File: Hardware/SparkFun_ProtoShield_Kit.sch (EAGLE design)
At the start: 27 parts

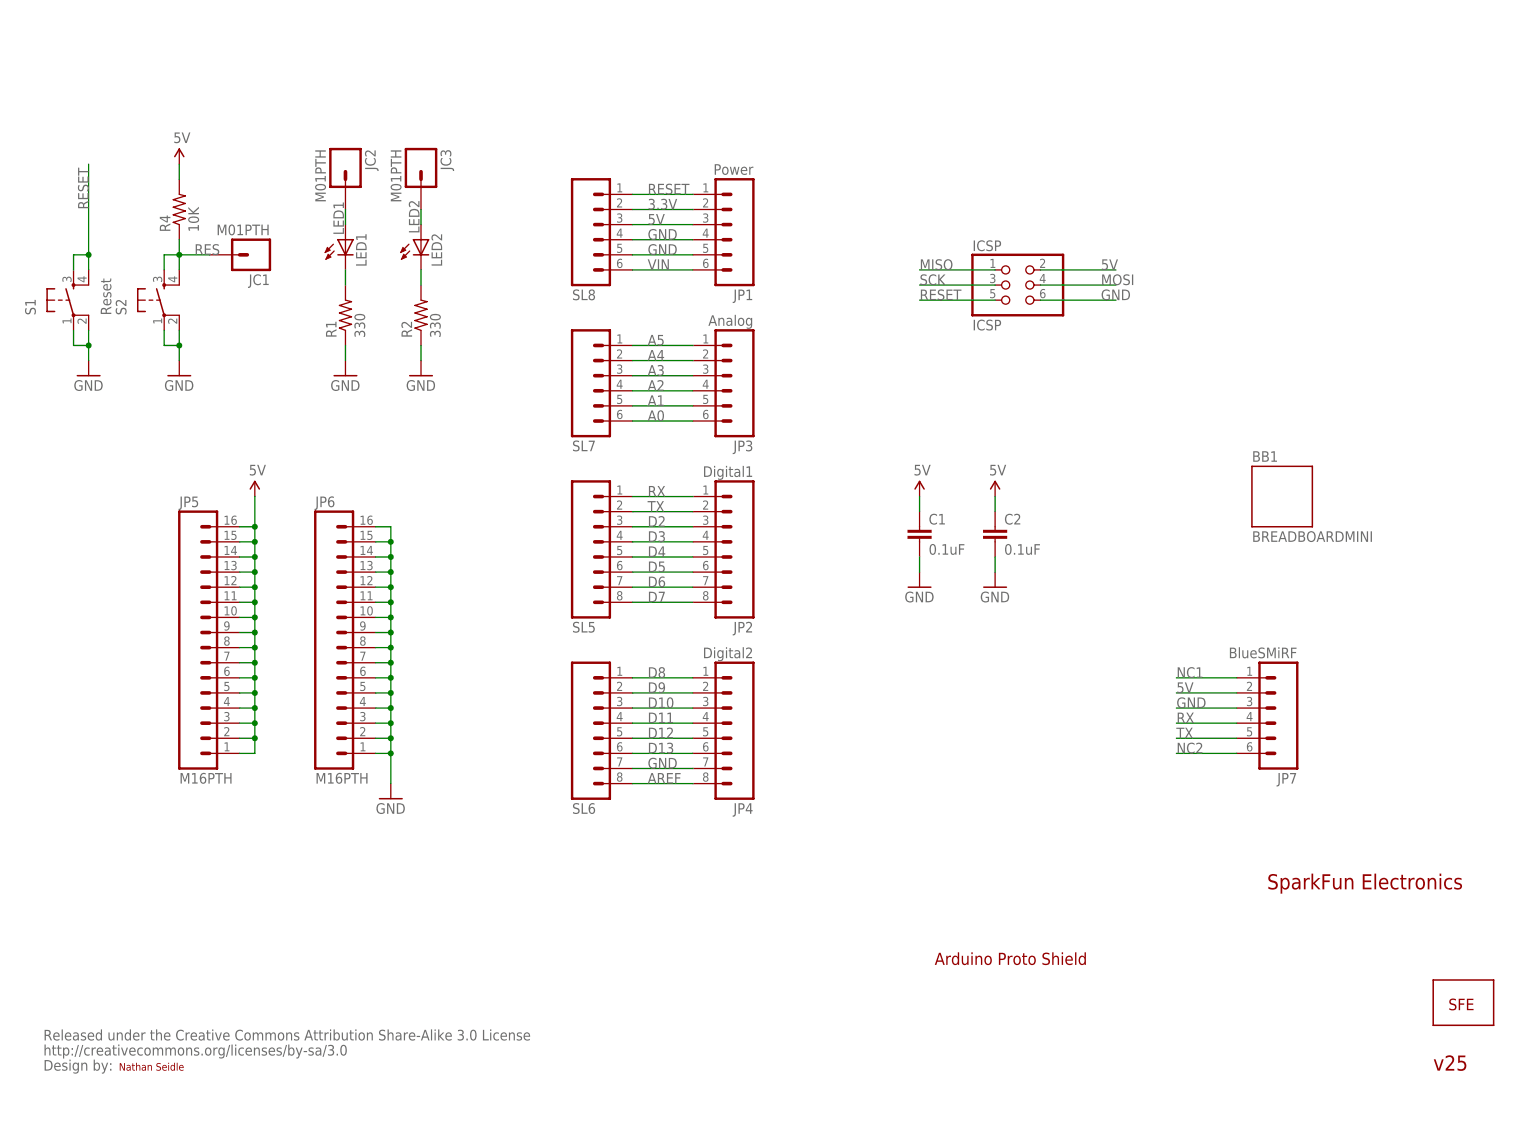
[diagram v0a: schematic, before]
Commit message: WIP - basic hardware layout changes
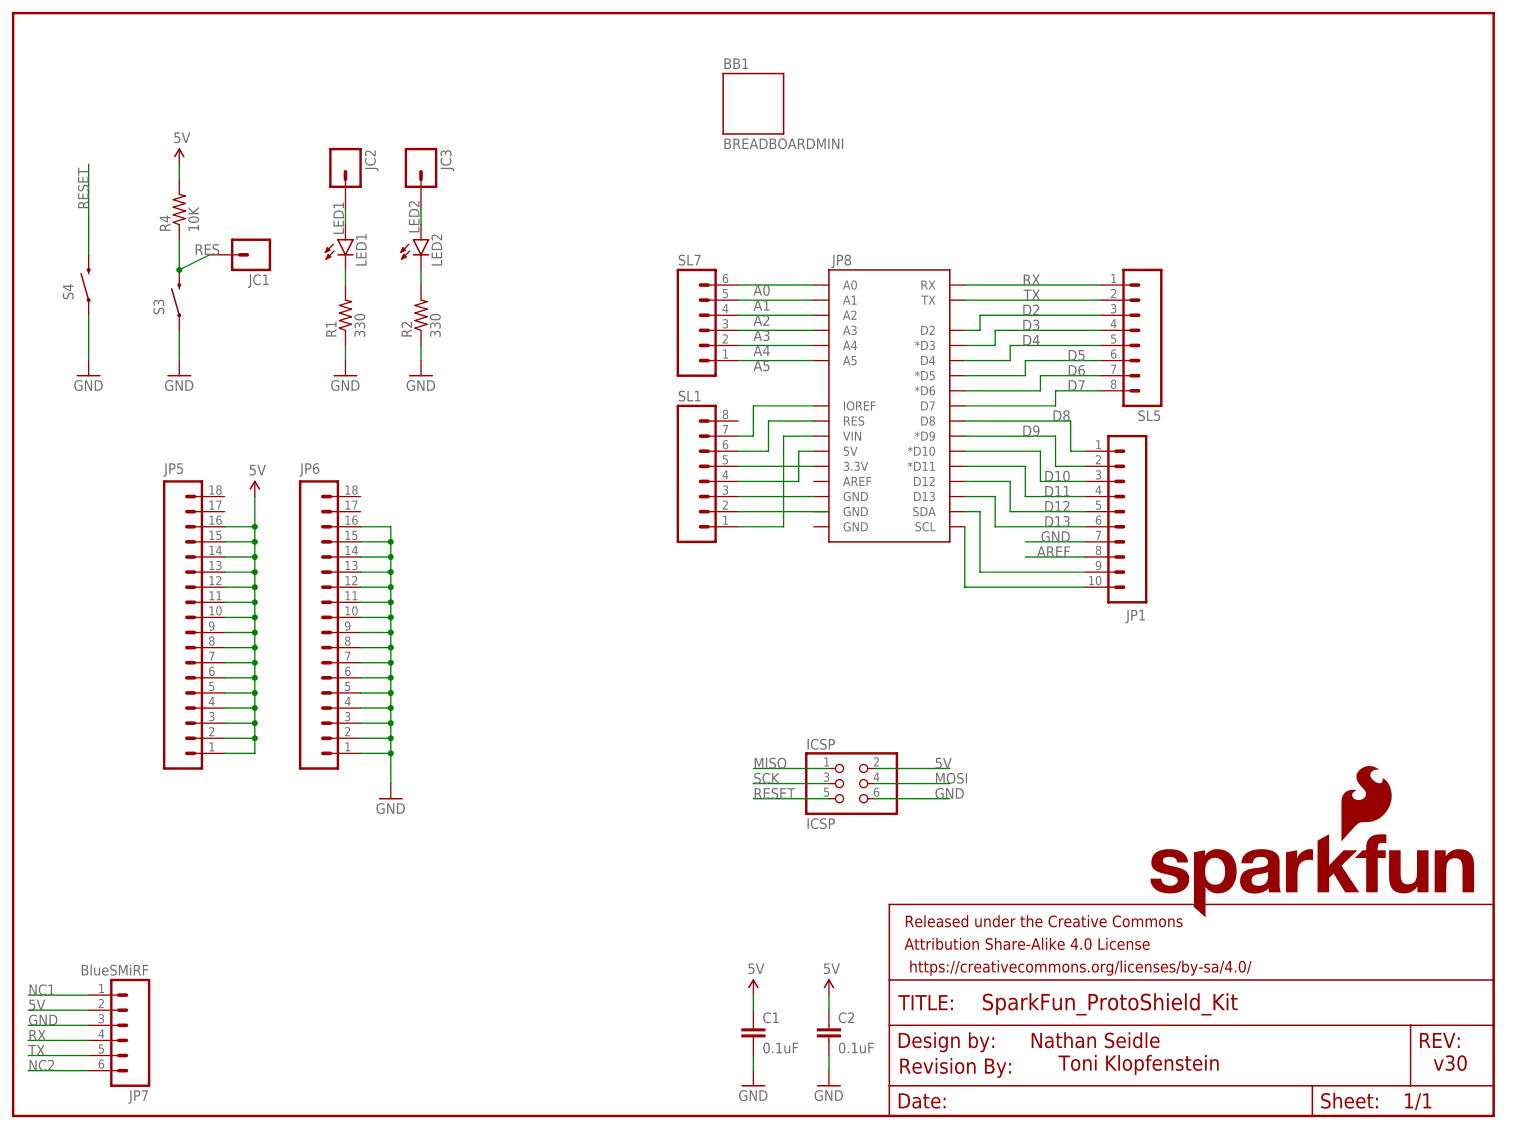
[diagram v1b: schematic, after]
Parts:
- removed JP2: Digital1, SparkFun:M08
- removed JP3: Analog, SparkFun:M06SIP
- removed JP4: Digital2, SparkFun:M08
- removed S1: Reset, SparkFun:TAC_SWITCHPTH
- removed S2: (no value), SparkFun:TAC_SWITCHPTH
- removed SL6: (no value), SparkFun:M08
- removed SL8: (no value), SparkFun:M06SIP
- added FRAME1: FRAME-LETTER, SparkFun-Aesthetics:FRAME-LETTER
- added JP8: ARDUINO_R3_SHIELDR3_PROTO_SHIELD, TempLibrary:ARDUINO_R3_SHIELDR3_PROTO_SHIELD
- added S3, S4: SWITCH-MOMENTARY-2PTH, SparkFun-Electromechanical:SWITCH-MOMENTARY-2PTH
- added SL1: (no value), SparkFun:M08
- JC1, JC2, JC3: value M01PTH -> (none); device SparkFun:M01PTH -> SparkFun-Connectors:M01PTH
- JP1: value Power -> (none); device SparkFun:M06SIP -> SparkFun-Connectors:M10SILK_FEMALE_PTH
- JP5, JP6: value M16PTH -> (none); device SparkFun:M16PTH -> TempLibrary:M18"
- LED1, LED2: device SparkFun:LED5MM -> SparkFun-LED:LED3MM
- U$1: value LOGO-SFENEW -> SFE_LOGO_NAME_FLAME.1_INCH; device SparkFun:LOGO-SFENEW -> SparkFun-Aesthetics:SFE_LOGO_NAME_FLAME.1_INCH
- U$2: value CREATIVE_COMMONS -> REVISION; device SparkFun:CREATIVE_COMMONS -> SparkFun-Aesthetics:REVISION
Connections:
- removed net 3.3V: JP1.2, SL8.2
- removed net VIN: JP1.6, SL8.6
- new net N$1: JP8.IOREF, SL1.7
- new net N$183: JP8.GND@2, SL1.3
- new net N$184: SL1.2
- new net N$185: JP8.VIN, SL1.1
- new net N$186: JP1.9, JP8.SDA
- new net N$187: JP1.10, JP8.SCL
- new net N$2: JP8.RES, SL1.6
- new net N$8: JP8.3.3V, SL1.5
- new net N$9: JP8.5V, SL1.4
- net 5V: no longer JP1.3, SL8.3
- net A0: now also JP8.A0; no longer JP3.6
- net A1: now also JP8.A1; no longer JP3.5
- net A2: now also JP8.A2; no longer JP3.4
- net A3: now also JP8.A3; no longer JP3.3
- net A4: now also JP8.A4; no longer JP3.2
- net A5: now also JP8.A5; no longer JP3.1
- net AREF: now also JP1.8; no longer JP4.8, SL6.8
- net D10: now also JP1.3, JP8.*D10; no longer JP4.3, SL6.3
- net D11: now also JP1.4, JP8.*D11; no longer JP4.4, SL6.4
- net D12: now also JP1.5, JP8.D12; no longer JP4.5, SL6.5
- net D13: now also JP1.6, JP8.D13; no longer JP4.6, SL6.6
- net D2: now also JP8.D2; no longer JP2.3
- net D3: now also JP8.*D3; no longer JP2.4
- net D4: now also JP8.D4; no longer JP2.5
- net D5: now also JP8.*D5; no longer JP2.6
- net D6: now also JP8.*D6; no longer JP2.7
- net D7: now also JP8.D7; no longer JP2.8
- net D8: now also JP1.1, JP8.D8; no longer JP4.1, SL6.1
- net D9: now also JP1.2, JP8.*D9; no longer JP4.2, SL6.2
- net GND: now also JP1.7, S3.1, S4.1; no longer JP1.4, JP1.5, JP4.7, S1.1, S1.2, S2.1, S2.2, SL6.7, SL8.4, SL8.5
- net RES: now also S3.2; no longer S2.3, S2.4
- net RESET: now also S4.2; no longer JP1.1, S1.3, S1.4, SL8.1
- net RX: now also JP8.RX; no longer JP2.1
- net TX: now also JP8.TX; no longer JP2.2
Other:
- note added: "Toni Klopfenstein"
- note added: "v30"
- note removed: "Arduino Proto Shield"
- note removed: "SparkFun Electronics"
- note removed: "v25"
- moved on the sheet: BB1, C1, C2, ICSP, JP7, SL5, SL7

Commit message: Ready for engineering review
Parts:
- added LOGO1: OSHW-LOGOS, SparkFun-Aesthetics:OSHW-LOGOS
- added SJ1, SJ2, SJ3, SJ4: JUMPER-PAD-2-NC_BY_TRACE, SparkFun-Passives:JUMPER-PAD-2-NC_BY_TRACE
- JP5, JP6: device TempLibrary:M18" -> SparkFun-Connectors:M191X19
- U$1: value SFE_LOGO_NAME_FLAME.1_INCH -> SFE_LOGO_NAME.1_INCH; device SparkFun-Aesthetics:SFE_LOGO_NAME_FLAME.1_INCH -> SparkFun-Aesthetics:SFE_LOGO_NAME.1_INCH
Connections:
- net N$186 renamed SDA
- net N$187 renamed SCL
- removed net N$183: JP8.GND@2, SL1.3
- removed net N$184: SL1.2
- new net N$219: JP7.3, SJ3.1
- new net N$220: JP7.2, SJ4.1
- new net NC3: SL1.8
- net 5V: now also JP5.17, JP5.18, JP5.19, JP8.5V, SJ4.2, SL1.4; no longer JP7.2
- net AREF: now also JP8.AREF
- net GND: now also JP6.17, JP6.18, JP6.19, JP8.GND@0, JP8.GND@1, JP8.GND@2, SJ3.2, SL1.2, SL1.3; no longer JP7.3
- net N$2: now also JP7.5, SJ1.1; no longer JP8.RES, SL1.6
- net N$9: now also JP7.4, SJ2.1; no longer JP8.5V, SL1.4
- net RESET: now also JP8.RES, SL1.6
- net RX: now also SJ2.2; no longer JP7.4
- net TX: now also SJ1.2; no longer JP7.5
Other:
- note added: "Arduino Connections"
- note added: "Arduino Headers Connections"
- note added: "BlueSMiRF Footprint"
- note added: "Breadboard Footprint"
- note added: "Disable jumpers 1-4 to create customizable 6-pin header for prototyping."
- note added: "Prototyping Hardware"
- moved on the sheet: BB1, C1, C2, ICSP, JC1, JC2, JC3, JP1, JP7, JP8, LED1, LED2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

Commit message: Fixing part names, adding additional connector from engineering review
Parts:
- removed C1, C2: 0.1uF, SparkFun:CAPPTH2
- removed SL1, SL5: (no value), SparkFun:M08
- removed SL7: (no value), SparkFun:M06SIP
- added JP10, JP2: (no value), SparkFun-Connectors:M06SILK_FEMALE_PTH
- added JP11, JP12: (no value), SparkFun-Connectors:M08
- JP7: device SparkFun:M06SIP -> SparkFun-Connectors:M06SILK_FEMALE_PTH
- renumbered JC1 to JP3, JC2 to JP4, JC3 to JP9
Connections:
- removed net N$2: JP7.5, SJ1.1
- removed net N$219: JP7.3, SJ3.1
- removed net N$220: JP7.2, SJ4.1
- removed net N$9: JP7.4, SJ2.1
- new net FTDI_5V: JP2.2, JP7.2, SJ4.1
- new net FTDI_GND: JP2.3, JP7.3, SJ3.1
- new net FTDI_RX: JP2.4, JP7.4, SJ2.1
- new net FTDI_TX: JP2.5, JP7.5, SJ1.1
- net 5V: now also JP11.4; no longer C1.1, C2.1, SL1.4
- net A0: now also JP10.6; no longer SL7.6
- net A1: now also JP10.5; no longer SL7.5
- net A2: now also JP10.4; no longer SL7.4
- net A3: now also JP10.3; no longer SL7.3
- net A4: now also JP10.2; no longer SL7.2
- net A5: now also JP10.1; no longer SL7.1
- net D2: now also JP12.3; no longer SL5.3
- net D3: now also JP12.4; no longer SL5.4
- net D4: now also JP12.5; no longer SL5.5
- net D5: now also JP12.6; no longer SL5.6
- net D6: now also JP12.7; no longer SL5.7
- net D7: now also JP12.8; no longer SL5.8
- net GND: now also JP11.2, JP11.3; no longer C1.2, C2.2, SL1.2, SL1.3
- net N$1: now also JP11.7; no longer SL1.7
- net N$185: now also JP11.1; no longer SL1.1
- net N$8: now also JP11.5; no longer SL1.5
- net NC1: now also JP2.1
- net NC2: now also JP2.6
- net NC3: now also JP11.8; no longer SL1.8
- net RESET: now also JP11.6; no longer SL1.6
- net RX: now also JP12.1; no longer SL5.1
- net TX: now also JP12.2; no longer SL5.2
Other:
- moved on the sheet: BB1, JP7, SJ1, SJ2, SJ3, SJ4

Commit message: Updates from engineering review
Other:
- moved on the sheet: JP2, JP7, SJ1, SJ2, SJ3, SJ4

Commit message: Updates from checklist
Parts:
- BB1: device SparkFun:BREADBOARDMINI -> SparkFun-Boards:BREADBOARDMINI
- ICSP: device pinhead:PINHD-2X3 -> SparkFun-Connectors:AVR_SPI_PRG_6PTH
- R1, R2, R4: device SparkFun:RESISTORPTH1 -> SparkFun-Resistors:RESISTORAXIAL-0.3
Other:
- moved on the sheet: S3
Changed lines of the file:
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@@
 <?xml version="1.0" encoding="utf-8"?>
 <!DOCTYPE eagle SYSTEM "eagle.dtd">
-<eagle version="7.4.0">
+<eagle version="7.5.0">
 <drawing>
 <settings>
@@
 </classes>
 <parts>
-<part name="ICSP" library="pinhead" deviceset="PINHD-2X3" device="" value="ICSP"/>
-<part name="R1" library="SparkFun" deviceset="RESISTOR" device="PTH1" value="330"/>
-<part name="R2" library="SparkFun" deviceset="RESISTOR" device="PTH1" value="330"/>
+<part name="ICSP" library="SparkFun-Connectors" deviceset="AVR_SPI_PRG_6" device="PTH" value="ICSP"/>
+<part name="R1" library="SparkFun-Resistors" deviceset="RESISTOR" device="AXIAL-0.3" value="330"/>
+<part name="R2" library="SparkFun-Resistors" deviceset="RESISTOR" device="AXIAL-0.3" value="330"/>
 <part name="LED1" library="SparkFun-LED" deviceset="LED" device="3MM"/>
 <part name="LED2" library="SparkFun-LED" deviceset="LED" device="3MM"/>
@@
 <part name="P+2" library="SparkFun-Aesthetics" deviceset="5V" device="" value="5V"/>
 <part name="GND4" library="SparkFun-Aesthetics" deviceset="GND" device=""/>
-<part name="BB1" library="SparkFun" deviceset="BREADBOARD" device="MINI"/>
-<part name="R4" library="SparkFun" deviceset="RESISTOR" device="PTH1" value="10K"/>
+<part name="BB1" library="SparkFun-Boards" deviceset="BREADBOARD" device="MINI"/>
+<part name="R4" library="SparkFun-Resistors" deviceset="RESISTOR" device="AXIAL-0.3" value="10K"/>
 <part name="GND5" library="SparkFun-Aesthetics" deviceset="GND" device=""/>
 <part name="JP3" library="SparkFun-Connectors" deviceset="M01" device="PTH"/>
@@
 </plain>
 <instances>
-<instance part="ICSP" gate="A" x="33.02" y="60.96"/>
+<instance part="ICSP" gate="G$1" x="33.02" y="60.96"/>
 <instance part="R1" gate="G$1" x="226.06" y="109.22" smashed="yes" rot="R90">
 <attribute name="NAME" x="224.5614" y="105.41" size="1.778" layer="95" rot="R90"/>
@@
 <instance part="JP11" gate="G$1" x="12.7" y="124.46"/>
 <instance part="JP1" gate="G$1" x="101.6" y="111.76" rot="R180"/>
-<instance part="S3" gate="G$1" x="198.12" y="111.76" smashed="yes" rot="R90">
-<attribute name="NAME" x="195.58" y="109.22" size="1.778" layer="95" rot="R90"/>
+<instance part="S3" gate="G$1" x="198.12" y="109.22" smashed="yes" rot="R90">
+<attribute name="NAME" x="195.58" y="106.68" size="1.778" layer="95" rot="R90"/>
 </instance>
 <instance part="S4" gate="G$1" x="71.12" y="68.58" smashed="yes" rot="R90">
@@
 </segment>
 <segment>
-<wire x1="198.12" y1="106.68" x2="198.12" y2="101.6" width="0.1524" layer="91"/>
+<wire x1="198.12" y1="104.14" x2="198.12" y2="101.6" width="0.1524" layer="91"/>
 <pinref part="GND5" gate="1" pin="GND"/>
 <pinref part="S3" gate="G$1" pin="1"/>
 </segment>
 <segment>
-<wire x1="38.1" y1="58.42" x2="50.8" y2="58.42" width="0.1524" layer="91"/>
-<pinref part="ICSP" gate="A" pin="6"/>
+<wire x1="43.18" y1="58.42" x2="50.8" y2="58.42" width="0.1524" layer="91"/>
+<pinref part="ICSP" gate="G$1" pin="6"/>
 <pinref part="GND10" gate="1" pin="GND"/>
 <wire x1="50.8" y1="58.42" x2="50.8" y2="55.88" width="0.1524" layer="91"/>
@@
 <net name="RESET" class="0">
 <segment>
-<wire x1="30.48" y1="58.42" x2="17.78" y2="58.42" width="0.1524" layer="91"/>
-<pinref part="ICSP" gate="A" pin="5"/>
+<wire x1="25.4" y1="58.42" x2="17.78" y2="58.42" width="0.1524" layer="91"/>
+<pinref part="ICSP" gate="G$1" pin="5"/>
 <label x="17.78" y="58.42" size="1.27" layer="95" rot="R180" xref="yes"/>
 </segment>
@@
 </segment>
 <segment>
-<wire x1="38.1" y1="63.5" x2="50.8" y2="63.5" width="0.1524" layer="91"/>
-<pinref part="ICSP" gate="A" pin="2"/>
+<wire x1="43.18" y1="63.5" x2="50.8" y2="63.5" width="0.1524" layer="91"/>
+<pinref part="ICSP" gate="G$1" pin="2"/>
 <pinref part="P+5" gate="G$1" pin="5V"/>
 <wire x1="50.8" y1="63.5" x2="50.8" y2="68.58" width="0.1524" layer="91"/>
@@
 <net name="RES" class="0">
 <segment>
-<wire x1="198.12" y1="116.84" x2="198.12" y2="121.92" width="0.1524" layer="91"/>
-<wire x1="198.12" y1="116.84" x2="203.2" y2="116.84" width="0.1524" layer="91"/>
+<wire x1="198.12" y1="114.3" x2="198.12" y2="116.84" width="0.1524" layer="91"/>
 <label x="200.66" y="116.84" size="1.778" layer="95"/>
 <pinref part="R4" gate="G$1" pin="1"/>
+<pinref part="S3" gate="G$1" pin="2"/>
 <pinref part="JP3" gate="G$1" pin="1"/>
-<pinref part="S3" gate="G$1" pin="2"/>
+<wire x1="198.12" y1="116.84" x2="198.12" y2="121.92" width="0.1524" layer="91"/>
+<wire x1="203.2" y1="116.84" x2="198.12" y2="116.84" width="0.1524" layer="91"/>
 <junction x="198.12" y="116.84"/>
 </segment>
@@
 <net name="MOSI" class="0">
 <segment>
-<wire x1="38.1" y1="60.96" x2="50.8" y2="60.96" width="0.1524" layer="91"/>
-<pinref part="ICSP" gate="A" pin="4"/>
+<wire x1="43.18" y1="60.96" x2="50.8" y2="60.96" width="0.1524" layer="91"/>
+<pinref part="ICSP" gate="G$1" pin="4"/>
 <label x="50.8" y="60.96" size="1.27" layer="95" xref="yes"/>
 </segment>
@@
 <net name="MISO" class="0">
 <segment>
-<wire x1="30.48" y1="63.5" x2="17.78" y2="63.5" width="0.1524" layer="91"/>
-<pinref part="ICSP" gate="A" pin="1"/>
+<wire x1="25.4" y1="63.5" x2="17.78" y2="63.5" width="0.1524" layer="91"/>
+<pinref part="ICSP" gate="G$1" pin="1"/>
 <label x="17.78" y="63.5" size="1.27" layer="95" rot="R180" xref="yes"/>
 </segment>
@@
 <net name="SCK" class="0">
 <segment>
-<wire x1="30.48" y1="60.96" x2="17.78" y2="60.96" width="0.1524" layer="91"/>
-<pinref part="ICSP" gate="A" pin="3"/>
+<wire x1="25.4" y1="60.96" x2="17.78" y2="60.96" width="0.1524" layer="91"/>
+<pinref part="ICSP" gate="G$1" pin="3"/>
 <label x="17.78" y="60.96" size="1.27" layer="95" rot="R180" xref="yes"/>
 </segment>
